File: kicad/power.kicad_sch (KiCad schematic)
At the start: 70 parts, among them J6 RTC Battery, U10 TPS62086, U11 TPS62825, U2 MIMXRT1171DVMAB, Y3 24MHz, Y4 32.768kHz

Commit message: added remaining footprints
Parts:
- C40, C41, C42, C45, C49, C50, C52, C57, C58, C59, C60, C63, C64, C66, C67, C68, C72, C73, C75, C78, C79, C80, C82, C83, C84, C85, C88: footprint (none) -> Capacitor_SMD:C_0201_0603Metric
- C43, C44, C47, C65, C71, C87, C90: footprint (none) -> Capacitor_SMD:C_0603_1608Metric
- C46, C48, C51, C55, C69, C70, C76, C81, C89: footprint (none) -> Capacitor_SMD:C_0402_1005Metric
- D2: footprint Package_TO_SOT_SMD:SOT-23 -> project_footprints:BAT54C
- FB2, FB3: footprint (none) -> Inductor_SMD:L_0402_1005Metric
- U2: footprint Package_BGA:MAPBGA-289_14x14mm_Layout17x17_P0.8mm -> project_footprints:MIMXRT1171DVMAB
- U9: value (none) -> LM66200; footprint (none) -> project_footprints:LM66200
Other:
- moved on the sheet: C40, C41, FB2, FB3

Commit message: removed USB host and 1.8V DAC
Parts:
- renumbered C40 to C38, C41 to C39, C42 to C40, C43 to C41, C44 to C42, C45 to C43, C46 to C44, C47 to C45, C48 to C46, C49 to C47, C50 to C48, C51 to C49, C52 to C50, C53 to C51, C54 to C52, C55 to C53, C56 to C54, C57 to C55, C58 to C56, C59 to C57, C60 to C58, C61 to C59, C62 to C60, C63 to C61, C64 to C62, C65 to C63, C66 to C64, C67 to C65, C68 to C66, C69 to C67, C70 to C68, C71 to C69, C72 to C70, C73 to C71, C74 to C72, C75 to C73, C76 to C74, C77 to C75, C78 to C76, C79 to C77, C80 to C78, C81 to C79, C82 to C80, C83 to C81, C84 to C82, C85 to C83, C86 to C84, C87 to C85, C88 to C86, C89 to C87, C90 to C88, J6 to J5, U2 to U1, U11 to U10, U9 to U8, U10 to U9

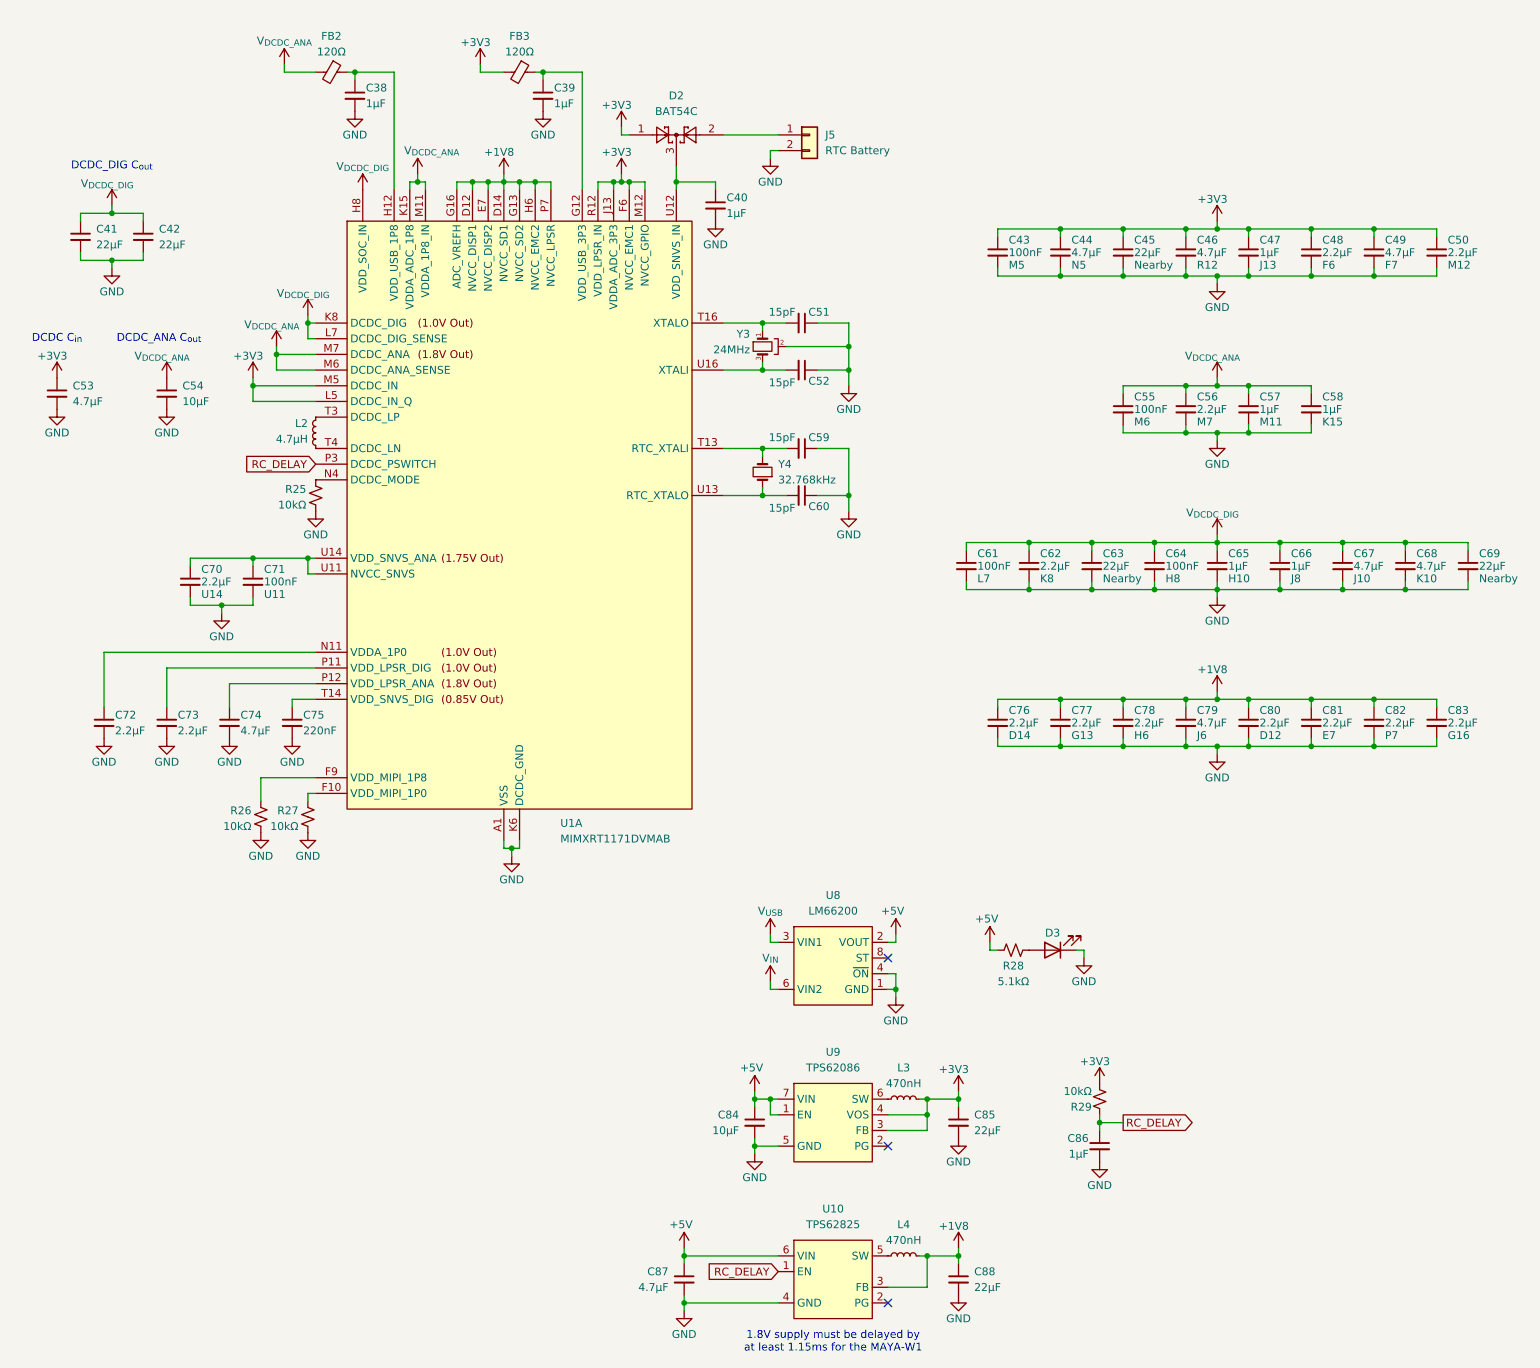
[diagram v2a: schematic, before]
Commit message: finished preliminary routing
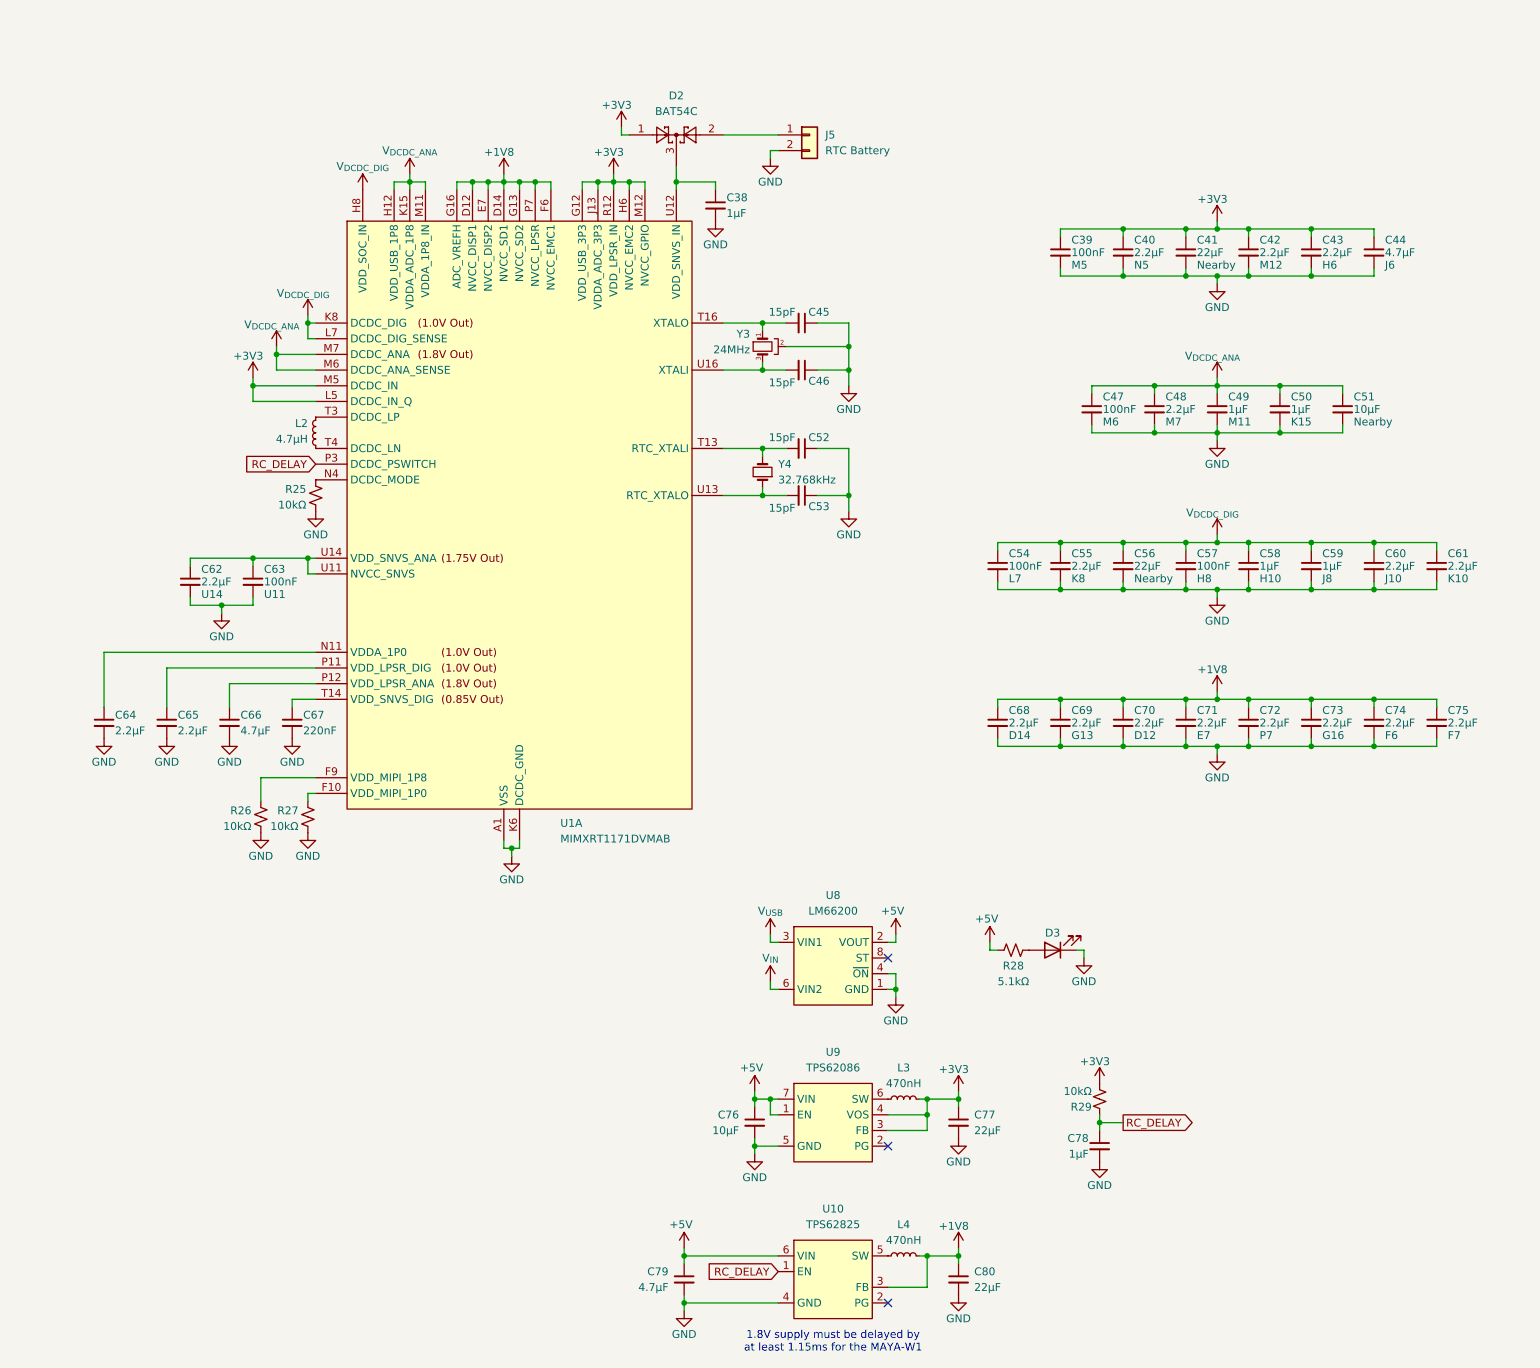
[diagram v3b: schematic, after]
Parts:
- removed C38, C39, C47: 1μF, Capacitor_SMD:C_0201_0603Metric, symbol Device:C_Small
- removed C41, C42, C69: 22μF, Capacitor_SMD:C_0603_1608Metric, symbol Device:C_Small
- removed C46, C53: 4.7μF, Capacitor_SMD:C_0402_1005Metric, symbol Device:C_Small
- removed FB2, FB3: 120Ω, Inductor_SMD:L_0402_1005Metric, symbol Device:FerriteBead_Small
- C40: renamed from C44; value 4.7μF -> 2.2μF; footprint Capacitor_SMD:C_0402_1005Metric -> Capacitor_SMD:C_0201_0603Metric
- C60: renamed from C67; value 4.7μF -> 2.2μF; footprint Capacitor_SMD:C_0402_1005Metric -> Capacitor_SMD:C_0201_0603Metric
- C61: renamed from C68; value 4.7μF -> 2.2μF; footprint Capacitor_SMD:C_0402_1005Metric -> Capacitor_SMD:C_0201_0603Metric
- C75: renamed from C49; value 4.7μF -> 2.2μF; footprint Capacitor_SMD:C_0402_1005Metric -> Capacitor_SMD:C_0201_0603Metric
- renumbered C40 to C38, C43 to C39, C45 to C41, C50 to C42, C78 to C43, C79 to C44, C51 to C45, C52 to C46, C55 to C47, C56 to C48, C57 to C49, C58 to C50, C54 to C51, C59 to C52, C60 to C53, C61 to C54, C62 to C55, C63 to C56, C64 to C57, C65 to C58, C66 to C59, C70 to C62, C71 to C63, C72 to C64, C73 to C65, C74 to C66, C75 to C67, C76 to C68, C77 to C69, C80 to C70, C81 to C71, C82 to C72, C83 to C73, C48 to C74, C84 to C76, C85 to C77, C86 to C78, C87 to C79, C88 to C80
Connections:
- net +1V8: now also C74.1, C75.1, U1.F6 (NVCC_EMC1), U1.F7 (NVCC_EMC1), U1.G6 (NVCC_EMC1); no longer C43.1, C44.1, U1.H6 (NVCC_EMC2), U1.J6 (NVCC_EMC2)
- net +3V3: now also C43.1, C44.1, U1.G12 (VDD_USB_3P3), U1.H6 (NVCC_EMC2), U1.J6 (NVCC_EMC2); no longer C74.1, C75.1, U1.F6 (NVCC_EMC1), U1.F7 (NVCC_EMC1), U1.G6 (NVCC_EMC1)
- net V_{DCDC_ANA}: now also U1.H12 (VDD_USB_1P8)
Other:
- note removed: "DCDC C_{in}"
- note removed: "DCDC_ANA C_{out}"
- note removed: "DCDC_DIG C_{out}"
- moved on the sheet: C39, C40, C41, C42, C43, C44, C47, C48, C49, C50, C51, C54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

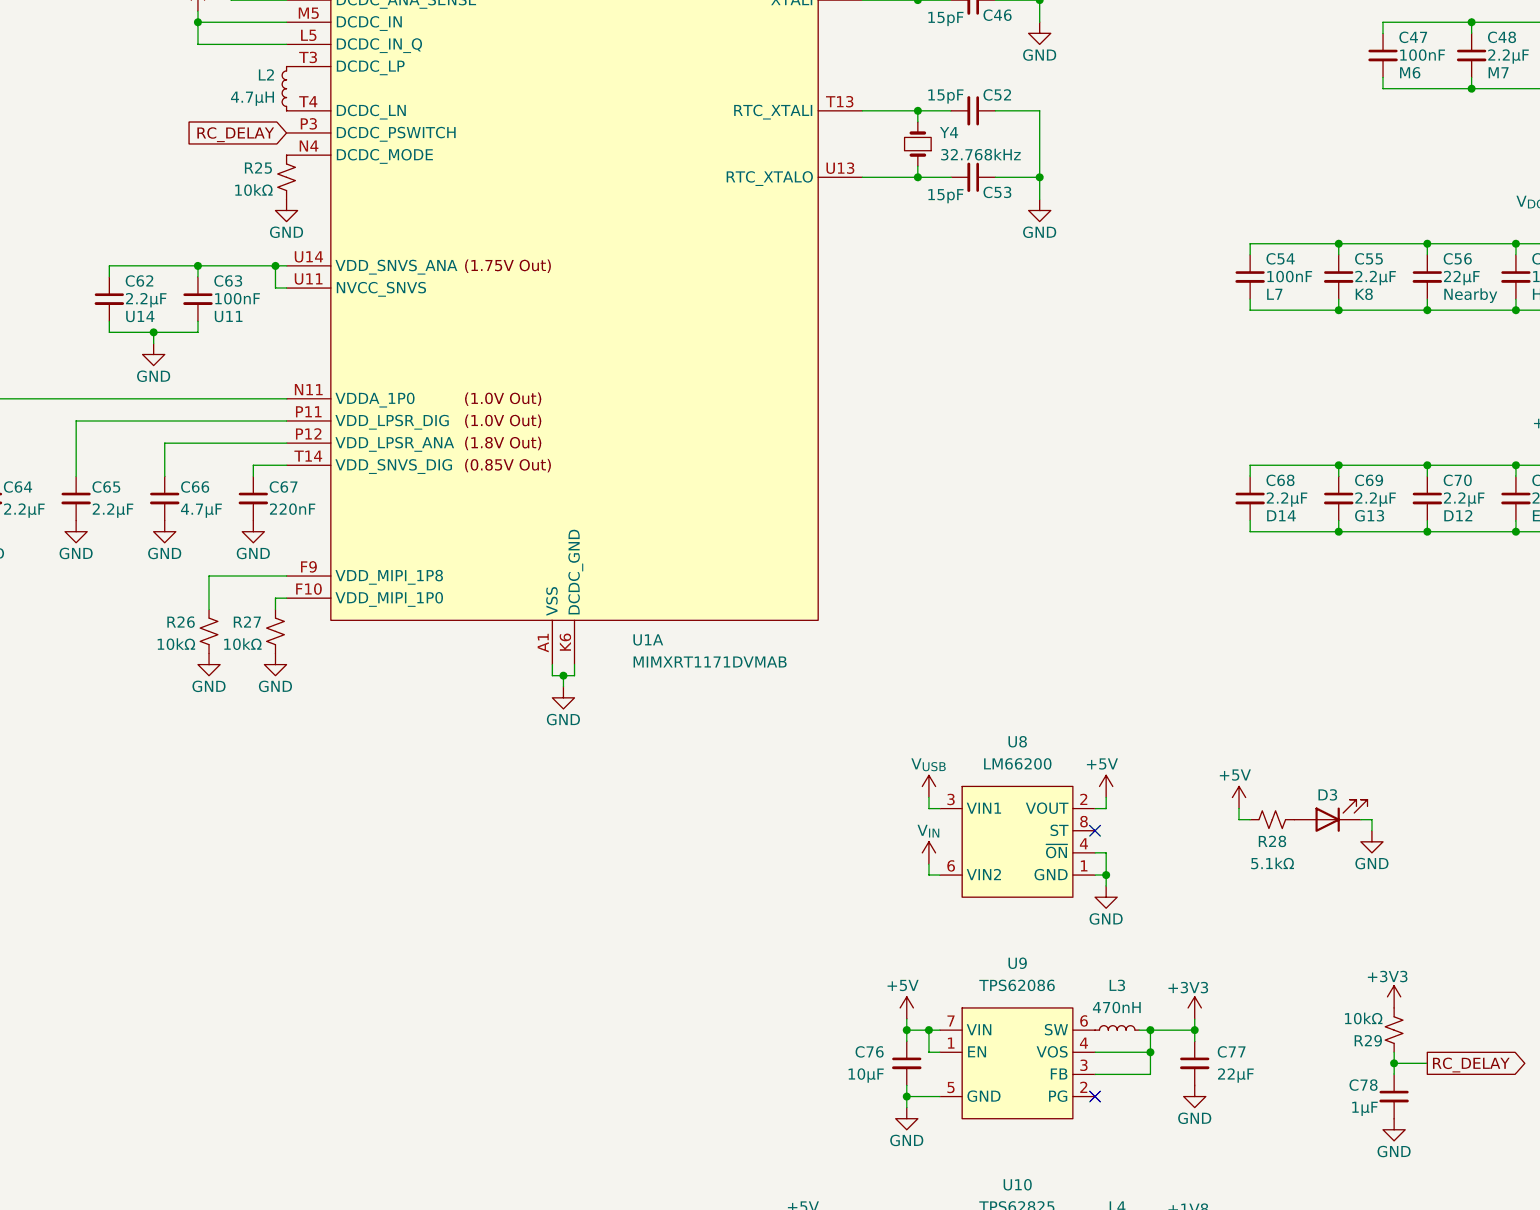
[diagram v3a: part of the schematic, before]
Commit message: added pull-up resistors to W25Q QSPI line
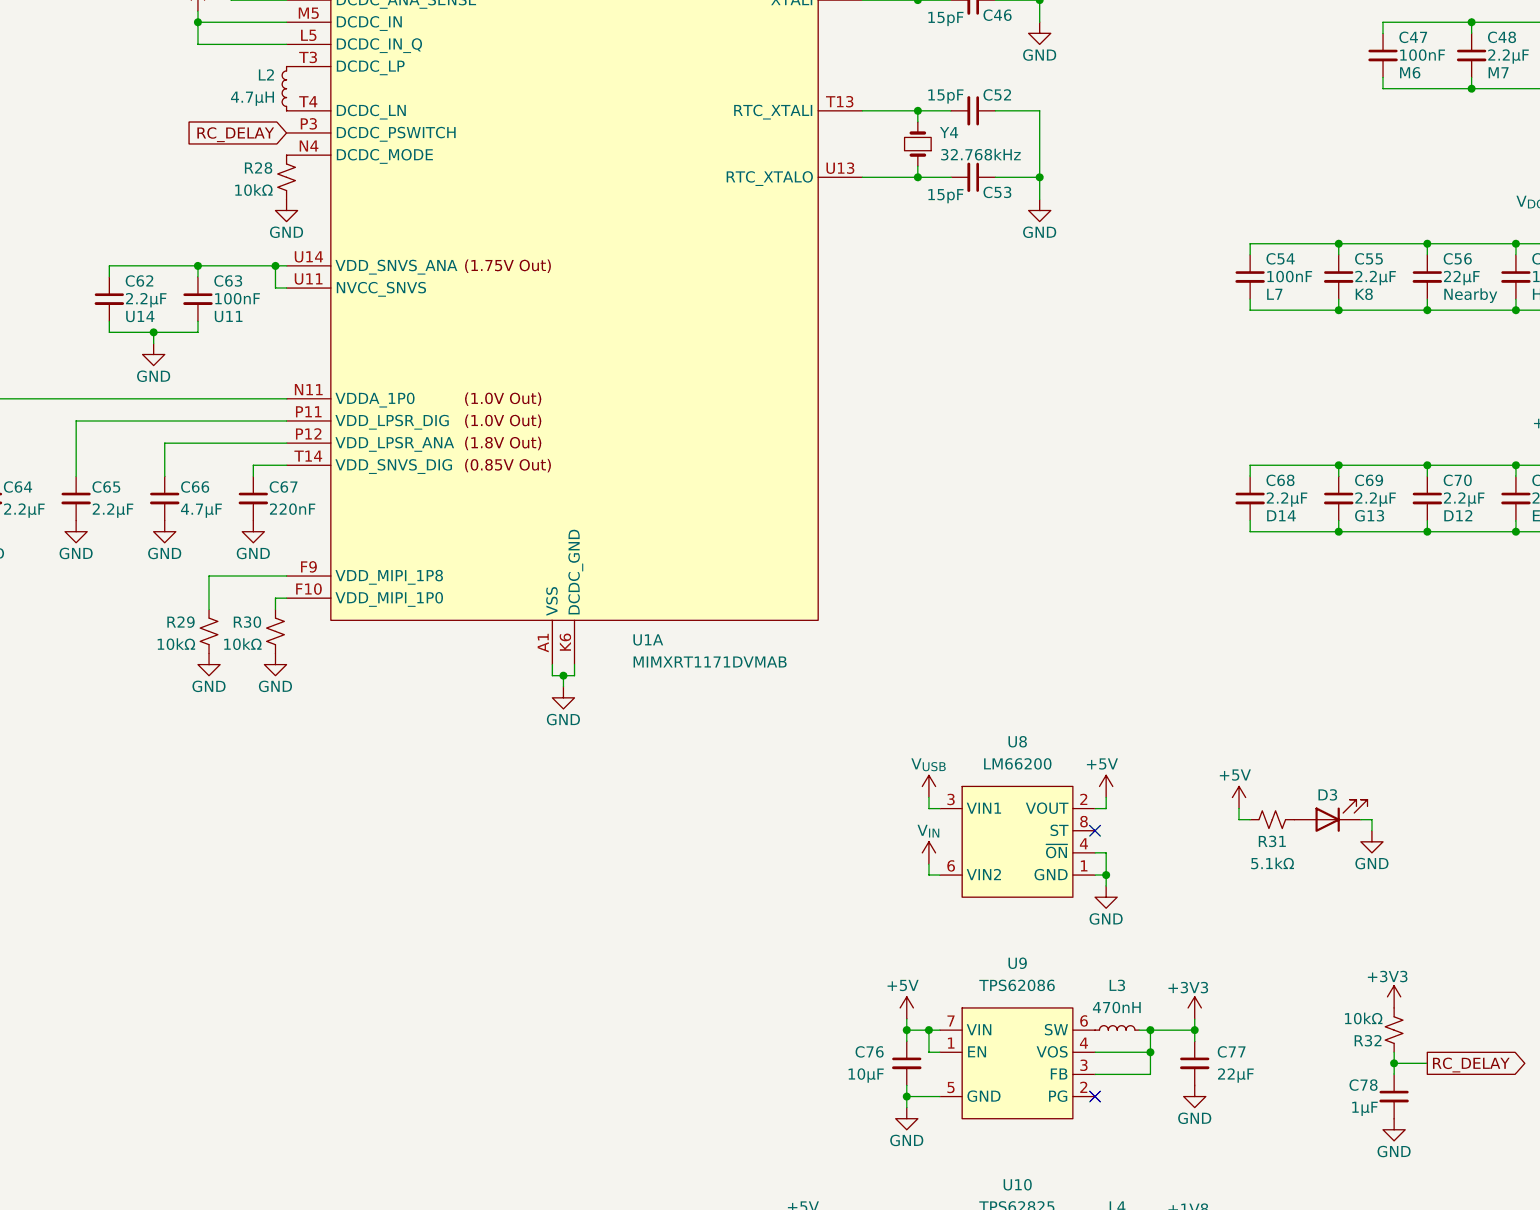
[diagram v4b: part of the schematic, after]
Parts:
- renumbered R25 to R28, R26 to R29, R27 to R30, R28 to R31, R29 to R32
